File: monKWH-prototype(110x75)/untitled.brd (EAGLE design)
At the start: 63 x 108 mm, 25 parts, among them X1 MSTBA2

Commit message: menambahkan komponen coaxial conn
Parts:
- added J1: U.FL-R-SMT(01), U.FL-R-SMT_01_:HRS_U.FL-R-SMT(01)
- moved R16 0.53 mm to (10.6, 53.2)
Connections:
- new net ANT: J1.3, LORA-NICERF-V1.ANT
- net GND: now also J1.1, J1.2
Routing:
- net GND: track 376.6 -> 397.0 mm, vias 4 -> 5
- net ANT: track 0.00 -> 7.86 mm, vias 0 -> 1
- net TX_DB9: track 68.8 -> 74.8 mm
- net LED_PROSES: track 116.5 -> 120.7 mm
- net SCK_VSPI: track 97.8 -> 101.9 mm
- net MISO_VSPI: track 68.1 -> 72.1 mm
- net MOSI_VSPI: track 87.1 -> 91.0 mm
- net RST_LORA: track 63.1 -> 66.5 mm
- net SS_LORA: track 83.5 -> 86.7 mm
- net LED_WARNING: track 55.3 -> 54.0 mm
- added copper zone on layer 16, net N$2
- added copper zone on layer 1, net N$9

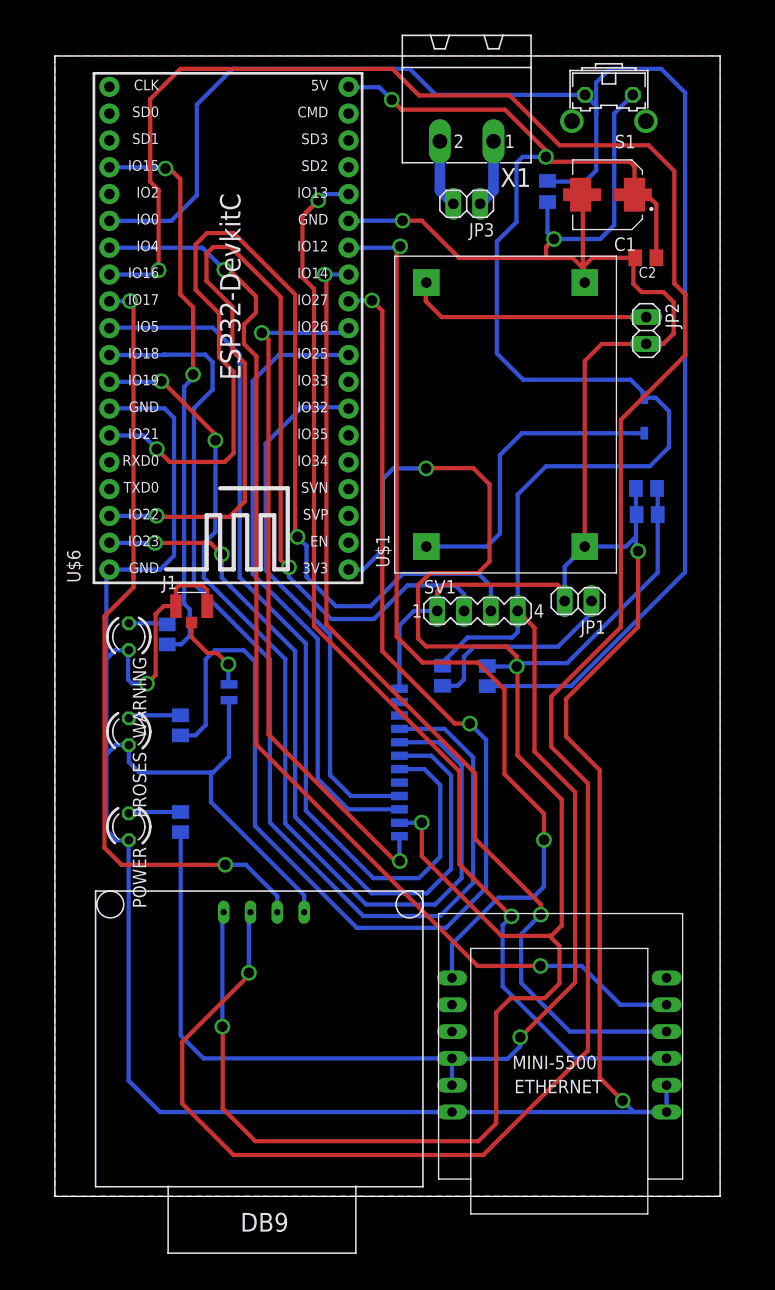
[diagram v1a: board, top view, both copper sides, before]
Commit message: revisi footprint LoRa
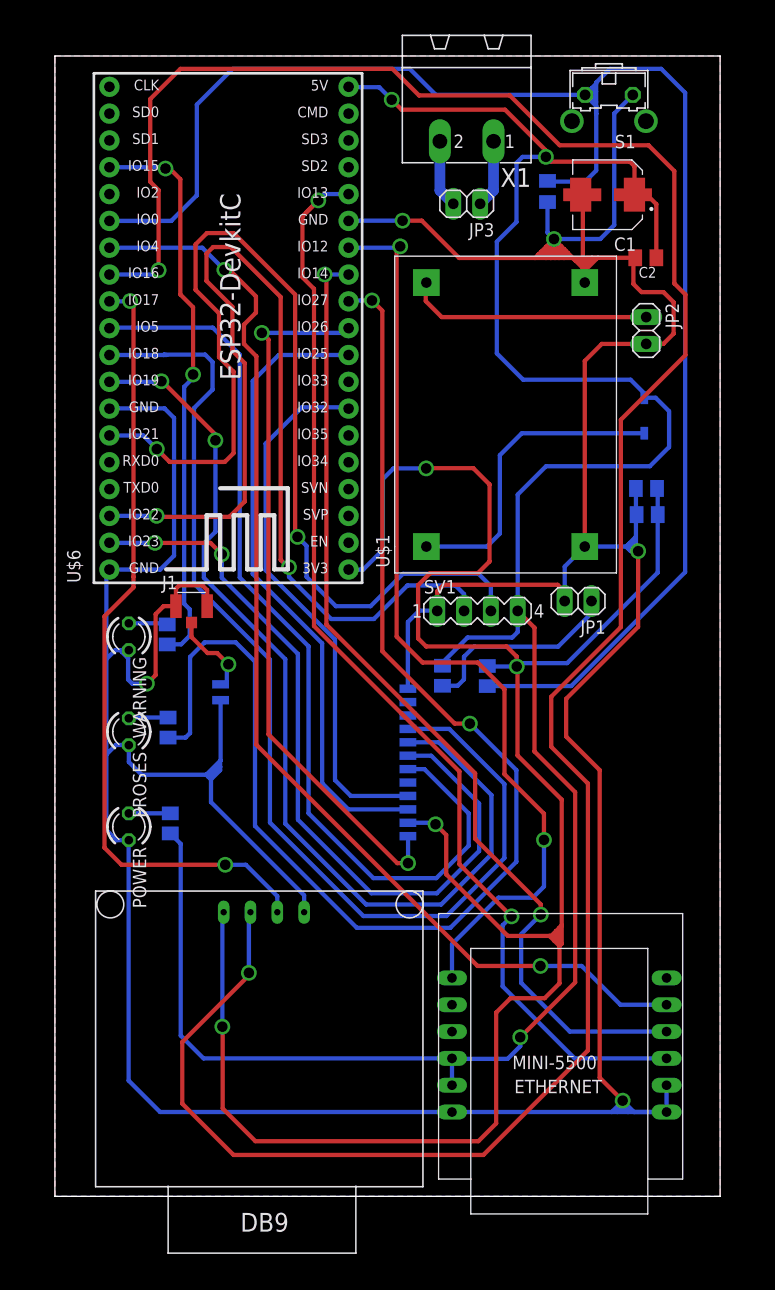
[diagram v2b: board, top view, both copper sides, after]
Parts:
- moved R3 1.20 mm to (10.7, 44.4)
- moved R1 0.97 mm to (10.9, 35.3)
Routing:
- net GND: track 397.0 -> 429.1 mm
- net LED_PROSES: track 120.7 -> 125.8 mm
- net 3V3: track 198.3 -> 203.3 mm
- net RST: track 151.2 -> 156.1 mm
- net SS_LORA: track 86.7 -> 89.1 mm
- net SCK_VSPI: track 101.9 -> 104.1 mm
- net MISO_VSPI: track 72.1 -> 74.1 mm
- net MOSI_VSPI: track 91.0 -> 92.9 mm
- net N$3: track 5.01 -> 3.75 mm
- net RST_LORA: track 66.5 -> 67.5 mm
- net N$1: track 4.94 -> 3.93 mm
- net LORA_DI1: track 50.6 -> 51.4 mm
- net LORA_DI0: track 59.3 -> 60.1 mm
- net ANT: track 7.86 -> 8.44 mm

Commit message: mengubah board
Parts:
- moved J1 3.00 mm to (12.9, 52.9)
- moved POWER 2.00 mm to (7.00, 33.0)
- moved U$6 1.06 mm to (16.2, 81.2)
- moved PROSES 1.00 mm to (7.00, 43.0)
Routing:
- net GND: track 429.1 -> 426.4 mm
- net TX_DB9: track 74.8 -> 77.2 mm
- net ANT: track 8.44 -> 6.39 mm
- net MOSI_HSPI: track 106.7 -> 104.9 mm
- net N$1: track 3.93 -> 4.76 mm
- net LORA_DI1: track 51.4 -> 50.8 mm
- net RX_DB9: track 232.0 -> 232.5 mm
- net 3V3: track 203.3 -> 203.9 mm
- net LORA_DI0: track 60.1 -> 59.5 mm
- net SCL: track 96.0 -> 96.6 mm
- net SCK_VSPI: track 104.1 -> 104.7 mm
- net MOSI_VSPI: track 92.9 -> 93.5 mm
- net MISO_HSPI: track 88.7 -> 89.3 mm
- net LED_PROSES: track 125.8 -> 126.4 mm
- net RST: track 156.1 -> 156.7 mm
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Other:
- board size 63 x 108 mm -> 69 x 109 mm

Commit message: revisi .brd
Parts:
- removed JP3: (no value), pinhead:1X02
- added JP4: (no value), pinhead:1X03
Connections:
- net N$5: now also JP4.3; no longer JP3.2
- net N$8: now also JP4.1; no longer JP3.1
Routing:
- net OUT+: track 224.5 -> 226.0 mm
- net RX_DB9: track 232.5 -> 233.6 mm
- net SS_LAN_CONV: track 108.0 -> 108.9 mm
- net GND: track 426.4 -> 425.8 mm
- net N$5: track 6.45 -> 5.89 mm
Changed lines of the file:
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@@
 <setting verticaltext="up"/>
 </settings>
-<grid distance="1" unitdist="mm" unit="mm" style="lines" multiple="1" display="yes" altdistance="5" altunitdist="mil" altunit="mil"/>
+<grid distance="0.003125" unitdist="mic" unit="mm" style="lines" multiple="1" display="yes" altdistance="5" altunitdist="mil" altunit="mil"/>
 <layers>
 <layer number="1" name="Top" color="4" fill="1" visible="yes" active="yes"/>
@@
 <attribute name="VALUE" x="44.08" y="105" size="1.778" layer="27" ratio="10" rot="R180"/>
 </element>
-<element name="JP3" library="pinhead" library_urn="urn:adsk.eagle:library:325" package="1X02" package3d_urn="urn:adsk.eagle:package:22435/2" value="" x="39" y="94" smashed="yes" rot="R180">
-<attribute name="NAME" x="41.6162" y="92.1712" size="1.27" layer="25" ratio="10" rot="R180"/>
-<attribute name="POPULARITY" value="98" x="39" y="94" size="1.778" layer="27" rot="R180" display="off"/>
-<attribute name="VALUE" x="41.54" y="97.175" size="1.27" layer="27" rot="R180"/>
-</element>
 <element name="POWER" library="led" library_urn="urn:adsk.eagle:library:259" package="LED3MM" package3d_urn="urn:adsk.eagle:package:15797/1" value="TLLR4400" x="7" y="33" smashed="yes" rot="R270">
 <attribute name="MF" value="VISHAY SEMICONDUCTOR" x="7" y="33" size="1.778" layer="27" rot="R270" display="off"/>
@@
 <attribute name="PURCHASE-URL" value="https://pricing.snapeda.com/search/part/U.FL-R-SMT(01)/?ref=eda" x="12.941" y="52.894415625" size="1.778" layer="27" display="off"/>
 <attribute name="VALUE" x="9.733959375" y="49.086065625" size="1.272709375" layer="27"/>
+</element>
+<element name="JP4" library="pinhead" library_urn="urn:adsk.eagle:library:325" package="1X03" package3d_urn="urn:adsk.eagle:package:22458/2" value="" x="39.03086875" y="94.038975" smashed="yes" rot="R180">
+<attribute name="NAME" x="42.91706875" y="92.210175" size="1.27" layer="25" ratio="10" rot="R180"/>
+<attribute name="POPULARITY" value="92" x="39.03086875" y="94.038975" size="1.778" layer="27" rot="R180" display="off"/>
+<attribute name="VALUE" x="42.84086875" y="97.213975" size="1.27" layer="27" rot="R180"/>
 </element>
 </elements>
@@
 <wire x1="5.013496875" y1="58.3094125" x2="8.918346875" y2="58.3094125" width="0.4064" layer="16"/>
 <wire x1="8.918346875" y1="58.3094125" x2="11.285346875" y2="60.6764125" width="0.4064" layer="16"/>
-<wire x1="11.285346875" y1="60.6764125" x2="11.285346875" y2="73.7191625" width="0.4064" layer="16"/>
-<wire x1="11.285346875" y1="73.7191625" x2="10.813259375" y2="74.19125" width="0.4064" layer="16"/>
-<wire x1="10.813259375" y1="74.19125" x2="5.655334375" y2="74.19125" width="0.4064" layer="16"/>
+<wire x1="11.285346875" y1="60.6764125" x2="11.285346875" y2="72.655590625" width="0.4064" layer="16"/>
+<wire x1="11.285346875" y1="72.655590625" x2="9.7496875" y2="74.19125" width="0.4064" layer="16"/>
+<wire x1="9.7496875" y1="74.19125" x2="5.655334375" y2="74.19125" width="0.4064" layer="16"/>
 <wire x1="5.655334375" y1="74.19125" x2="5.013496875" y2="73.5494125" width="0.4064" layer="16"/>
 <wire x1="55.026525" y1="62.471025" x2="55.026525" y2="64.62975" width="0.4064" layer="16"/>
@@
 <wire x1="10.588753125" y1="79.681428125" x2="10.3059625" y2="79.681428125" width="0.4064" layer="16"/>
 <wire x1="9.253946875" y1="78.6294125" x2="5.013496875" y2="78.6294125" width="0.4064" layer="16"/>
-<wire x1="20.363825" y1="50.83985625" x2="13.1723625" y2="58.03131875" width="0.4064" layer="16"/>
-<wire x1="13.1723625" y1="58.03131875" x2="13.1723625" y2="74.643990625" width="0.4064" layer="16"/>
-<wire x1="13.1723625" y1="74.643990625" x2="14.931284375" y2="76.4029125" width="0.4064" layer="16"/>
+<wire x1="20.363825" y1="50.83985625" x2="13.299659375" y2="57.904021875" width="0.4064" layer="16"/>
+<wire x1="13.299659375" y1="57.904021875" x2="13.299659375" y2="74.7712875" width="0.4064" layer="16"/>
+<wire x1="13.299659375" y1="74.7712875" x2="14.931284375" y2="76.4029125" width="0.4064" layer="16"/>
 <wire x1="14.931284375" y1="76.4029125" x2="14.931284375" y2="79.0150875" width="0.4064" layer="16"/>
 <wire x1="14.931284375" y1="79.0150875" x2="14.227475" y2="79.718896875" width="0.4064" layer="16"/>
@@
 <wire x1="8.987059375" y1="76.0894125" x2="5.013496875" y2="76.0894125" width="0.4064" layer="16"/>
 <wire x1="15.202978125" y1="71.60230625" x2="15.202978125" y2="62.935034375" width="0.4064" layer="16"/>
-<wire x1="15.202978125" y1="62.935034375" x2="14.108415625" y2="61.840471875" width="0.4064" layer="16"/>
-<wire x1="14.108415625" y1="61.840471875" x2="14.108415625" y2="58.5786875" width="0.4064" layer="16"/>
-<wire x1="14.108415625" y1="58.5786875" x2="21.8190625" y2="50.868040625" width="0.4064" layer="16"/>
+<wire x1="15.202978125" y1="62.935034375" x2="14.337546875" y2="62.069603125" width="0.4064" layer="16"/>
+<wire x1="14.337546875" y1="62.069603125" x2="14.337546875" y2="58.34955625" width="0.4064" layer="16"/>
+<wire x1="14.337546875" y1="58.34955625" x2="21.8190625" y2="50.868040625" width="0.4064" layer="16"/>
 </signal>
 <signal name="TX_DB9">
@@
 <wire x1="40.575978125" y1="3.917015625" x2="16.921465625" y2="3.917015625" width="0.4064" layer="1"/>
 <wire x1="16.921465625" y1="3.917015625" x2="12.06436875" y2="8.7741125" width="0.4064" layer="1"/>
-<wire x1="12.06436875" y1="8.7741125" x2="12.06436875" y2="14.622046875" width="0.4064" layer="1"/>
-<wire x1="18.373196875" y1="20.930875" x2="12.06436875" y2="14.622046875" width="0.4064" layer="1"/>
-<wire x1="18.373196875" y1="20.930875" x2="18.373196875" y2="21.1672125" width="0.4064" layer="1"/>
+<wire x1="12.06436875" y1="8.7741125" x2="12.06436875" y2="16.7453875" width="0.4064" layer="1"/>
+<wire x1="18.373196875" y1="21.1672125" x2="16.48619375" y2="21.1672125" width="0.4064" layer="1"/>
+<wire x1="16.48619375" y1="21.1672125" x2="12.06436875" y2="16.7453875" width="0.4064" layer="1"/>
 <via x="18.373196875" y="21.1672125" extent="1-16" drill="1"/>
 <wire x1="18.373196875" y1="21.1672125" x2="18.373196875" y2="26.761553125" width="0.4064" layer="16"/>
@@
 <wire x1="16.050415625" y1="87.7489875" x2="16.080134375" y2="87.7489875" width="0.4064" layer="1"/>
 <via x="16.050415625" y="87.7489875" extent="1-16" drill="1"/>
-<wire x1="16.050415625" y1="87.7489875" x2="15.009990625" y2="88.7894125" width="0.4064" layer="16"/>
-<wire x1="15.009990625" y1="88.7894125" x2="5.013496875" y2="88.7894125" width="0.4064" layer="16"/>
+<wire x1="16.050415625" y1="87.7489875" x2="13.915525" y2="89.883878125" width="0.4064" layer="16"/>
+<wire x1="13.915525" y1="89.883878125" x2="7.304609375" y2="89.883878125" width="0.4064" layer="16"/>
+<wire x1="7.304609375" y1="89.883878125" x2="6.21014375" y2="88.7894125" width="0.4064" layer="16"/>
+<wire x1="6.21014375" y1="88.7894125" x2="5.013496875" y2="88.7894125" width="0.4064" layer="16"/>
 <wire x1="17.90650625" y1="80.72924375" x2="17.90650625" y2="82.553628125" width="0.4064" layer="1"/>
 <wire x1="17.90650625" y1="80.72924375" x2="19.081534375" y2="79.554215625" width="0.4064" layer="1"/>
@@
 <wire x1="43.8299" y1="55.4442875" x2="45.41666875" y2="53.85751875" width="0.4064" layer="1"/>
 <wire x1="45.41666875" y1="53.85751875" x2="45.41666875" y2="42.1332375" width="0.4064" layer="1"/>
-<wire x1="44.08118125" y1="15.07345" x2="44.0706375" y2="15.07345" width="0.4064" layer="1"/>
+<wire x1="46.65430625" y1="15.07345" x2="44.0706375" y2="15.07345" width="0.4064" layer="1"/>
 <via x="44.0706375" y="15.07345" extent="1-16" drill="1"/>
 <wire x1="44.0706375" y1="15.07345" x2="44.0706375" y2="14.2216875" width="0.4064" layer="16"/>
@@
 <wire x1="43.71201875" y1="97.867571875" x2="44.287434375" y2="98.4429875" width="0.4064" layer="16"/>
 <wire x1="44.287434375" y1="98.4429875" x2="46.501459375" y2="98.4429875" width="0.4064" layer="16"/>
-<wire x1="49.272290625" y1="20.264559375" x2="44.08118125" y2="15.07345" width="0.4064" layer="1"/>
-<wire x1="49.272290625" y1="38.277615625" x2="49.272290625" y2="20.264559375" width="0.4064" layer="1"/>
+<wire x1="49.272290625" y1="17.691434375" x2="46.65430625" y2="15.07345" width="0.4064" layer="1"/>
+<wire x1="49.272290625" y1="38.277615625" x2="49.272290625" y2="17.691434375" width="0.4064" layer="1"/>
 </signal>
 <signal name="N$4">
@@
 </signal>
 <signal name="N$5">
-<contactref element="JP3" pad="2"/>
 <contactref element="X1" pad="2"/>
-<wire x1="36.46" y1="99.92" x2="36.46" y2="95.27" width="1.016" layer="16"/>
-<wire x1="36.46" y1="95.27" x2="37.73" y2="94" width="1.016" layer="16"/>
+<wire x1="36.46" y1="99.92" x2="36.46" y2="95.803790625" width="1.016" layer="16"/>
+<contactref element="JP4" pad="3"/>
+<wire x1="36.46" y1="95.803790625" x2="36.46" y2="95.27" width="1.016" layer="16"/>
+<wire x1="36.46" y1="95.27" x2="36.46" y2="94.06984375" width="1.016" layer="16"/>
+<wire x1="36.46" y1="94.06984375" x2="36.49086875" y2="94.038975" width="1.016" layer="16"/>
 </signal>
 <signal name="N$8">
 <contactref element="X1" pad="1"/>
-<contactref element="JP3" pad="1"/>
-<wire x1="40.27" y1="94" x2="41.54" y2="95.27" width="1.016" layer="16"/>
-<wire x1="41.54" y1="95.27" x2="41.54" y2="99.92" width="1.016" layer="16"/>
+<wire x1="41.54" y1="95.27" x2="41.54" y2="95.9056" width="1.016" layer="16"/>
+<contactref element="JP4" pad="1"/>
+<wire x1="41.54" y1="95.9056" x2="41.54" y2="99.92" width="1.016" layer="16"/>
+<wire x1="41.57086875" y1="94.038975" x2="41.57086875" y2="95.87473125" width="1.016" layer="16"/>
+<wire x1="41.57086875" y1="95.87473125" x2="41.54" y2="95.9056" width="1.016" layer="16"/>
 </signal>
 <signal name="EN">
